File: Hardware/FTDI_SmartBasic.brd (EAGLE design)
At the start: 35.6 x 20.3 mm, 29 parts, among them U1 FT232RLSSOP, U2 MIC5219 3.3V, U3 TS3USB221A

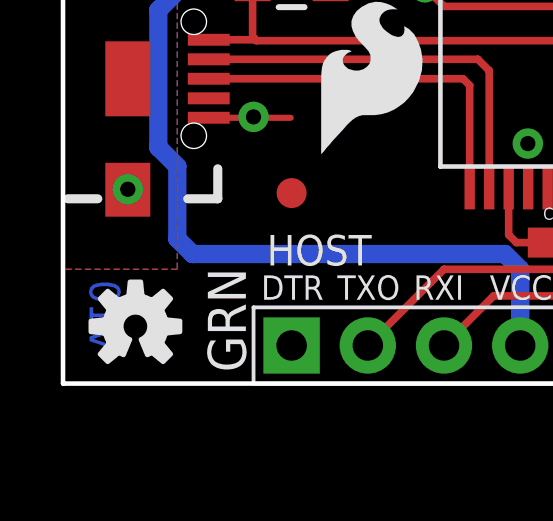
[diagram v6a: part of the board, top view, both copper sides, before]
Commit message: Fixed bottom silk, rev to 11
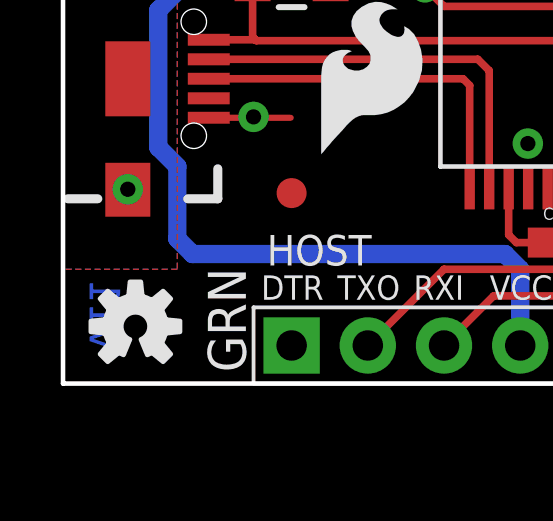
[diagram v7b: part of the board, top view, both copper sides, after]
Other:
- board text added: "v11"
- board text removed: "v10"
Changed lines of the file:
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@@
 <?xml version="1.0" encoding="utf-8"?>
 <!DOCTYPE eagle SYSTEM "eagle.dtd">
-<eagle version="6.6.0">
+<eagle version="6.5.0">
 <drawing>
 <settings>
@@
 <setting verticaltext="up"/>
 </settings>
-<grid distance="0.05" unitdist="inch" unit="inch" style="lines" multiple="1" display="yes" altdistance="0.01" altunitdist="inch" altunit="inch"/>
+<grid distance="0.05" unitdist="inch" unit="inch" style="lines" multiple="1" display="yes" altdistance="0.005" altunitdist="inch" altunit="inch"/>
 <layers>
-<layer number="1" name="Top" color="4" fill="1" visible="yes" active="yes"/>
-<layer number="2" name="Route2" color="1" fill="3" visible="yes" active="yes"/>
-<layer number="15" name="Route15" color="4" fill="6" visible="yes" active="yes"/>
+<layer number="1" name="Top" color="4" fill="1" visible="no" active="yes"/>
+<layer number="2" name="Route2" color="1" fill="3" visible="no" active="yes"/>
+<layer number="15" name="Route15" color="4" fill="6" visible="no" active="yes"/>
 <layer number="16" name="Bottom" color="1" fill="1" visible="yes" active="yes"/>
 <layer number="17" name="Pads" color="2" fill="1" visible="yes" active="yes"/>
@@
 <layer number="19" name="Unrouted" color="6" fill="1" visible="yes" active="yes"/>
 <layer number="20" name="Dimension" color="6" fill="1" visible="yes" active="yes"/>
-<layer number="21" name="tPlace" color="6" fill="1" visible="yes" active="yes"/>
-<layer number="22" name="bPlace" color="6" fill="1" visible="yes" active="yes"/>
-<layer number="23" name="tOrigins" color="15" fill="1" visible="yes" active="yes"/>
+<layer number="21" name="tPlace" color="16" fill="1" visible="no" active="yes"/>
+<layer number="22" name="bPlace" color="14" fill="1" visible="yes" active="yes"/>
+<layer number="23" name="tOrigins" color="15" fill="1" visible="no" active="yes"/>
 <layer number="24" name="bOrigins" color="15" fill="1" visible="yes" active="yes"/>
-<layer number="25" name="tNames" color="7" fill="1" visible="yes" active="yes"/>
-<layer number="26" name="bNames" color="7" fill="1" visible="yes" active="yes"/>
-<layer number="27" name="tValues" color="7" fill="1" visible="yes" active="yes"/>
-<layer number="28" name="bValues" color="7" fill="1" visible="yes" active="yes"/>
-<layer number="29" name="tStop" color="7" fill="3" visible="yes" active="yes"/>
-<layer number="30" name="bStop" color="7" fill="6" visible="yes" active="yes"/>
-<layer number="31" name="tCream" color="7" fill="4" visible="yes" active="yes"/>
-<layer number="32" name="bCream" color="7" fill="5" visible="yes" active="yes"/>
-<layer number="39" name="tKeepout" color="4" fill="11" visible="yes" active="yes"/>
-<layer number="40" name="bKeepout" color="1" fill="11" visible="yes" active="yes"/>
-<layer number="41" name="tRestrict" color="4" fill="10" visible="yes" active="yes"/>
-<layer number="42" name="bRestrict" color="1" fill="10" visible="yes" active="yes"/>
-<layer number="43" name="vRestrict" color="2" fill="10" visible="yes" active="yes"/>
-<layer number="44" name="Drills" color="7" fill="1" visible="yes" active="yes"/>
-<layer number="45" name="Holes" color="7" fill="1" visible="yes" active="yes"/>
-<layer number="46" name="Milling" color="3" fill="1" visible="yes" active="yes"/>
-<layer number="51" name="tDocu" color="6" fill="1" visible="yes" active="yes"/>
-<layer number="52" name="bDocu" color="7" fill="1" visible="yes" active="yes"/>
+<layer number="25" name="tNames" color="7" fill="1" visible="no" active="yes"/>
+<layer number="26" name="bNames" color="7" fill="1" visible="no" active="yes"/>
+<layer number="27" name="tValues" color="7" fill="1" visible="no" active="yes"/>
+<layer number="28" name="bValues" color="7" fill="1" visible="no" active="yes"/>
+<layer number="29" name="tStop" color="7" fill="3" visible="no" active="yes"/>
+<layer number="30" name="bStop" color="7" fill="6" visible="no" active="yes"/>
+<layer number="31" name="tCream" color="7" fill="4" visible="no" active="yes"/>
+<layer number="32" name="bCream" color="7" fill="5" visible="no" active="yes"/>
+<layer number="39" name="tKeepout" color="4" fill="11" visible="no" active="yes"/>
+<layer number="40" name="bKeepout" color="1" fill="11" visible="no" active="yes"/>
+<layer number="41" name="tRestrict" color="4" fill="10" visible="no" active="yes"/>
+<layer number="42" name="bRestrict" color="1" fill="10" visible="no" active="yes"/>
+<layer number="43" name="vRestrict" color="2" fill="10" visible="no" active="yes"/>
+<layer number="44" name="Drills" color="7" fill="1" visible="no" active="yes"/>
+<layer number="45" name="Holes" color="7" fill="1" visible="no" active="yes"/>
+<layer number="46" name="Milling" color="3" fill="1" visible="no" active="yes"/>
+<layer number="51" name="tDocu" color="6" fill="1" visible="no" active="yes"/>
+<layer number="52" name="bDocu" color="7" fill="1" visible="no" active="no"/>
 <layer number="3" name="Route3" color="4" fill="3" visible="no" active="no"/>
 <layer number="4" name="Route4" color="1" fill="4" visible="no" active="no"/>
@@
 <text x="9.652" y="18.796" size="0.8128" layer="21" font="vector" ratio="15" rot="R90" align="bottom-center">3.3V</text>
 <text x="9.652" y="16.383" size="0.8128" layer="21" font="vector" ratio="15" rot="R90" align="bottom-center">5V</text>
-<text x="1.905" y="2.286" size="1.016" layer="16" font="vector" ratio="15" rot="MR270" align="bottom-center">v10</text>
+<text x="1.905" y="2.286" size="1.016" layer="16" font="vector" ratio="15" rot="MR270" align="bottom-center">v11</text>
 <text x="7.62" y="2.54" size="0.8128" layer="22" font="vector" ratio="15" rot="MR0" align="bottom-center">DTR</text>
 <text x="10.16" y="2.54" size="0.8128" layer="22" font="vector" ratio="15" rot="MR0" align="bottom-center">TXO</text>
@@
 <text x="27.94" y="3.048" size="0.8636" layer="22" font="vector" ratio="15" rot="MR0" align="bottom-center">SEL</text>
 <text x="30.48" y="3.048" size="0.8636" layer="22" font="vector" ratio="15" rot="MR0" align="bottom-center">!OE</text>
-<text x="33.02" y="3.81" size="0.8636" layer="22" font="vector" ratio="15" rot="SMR270" align="bottom-center">DTR</text>
-<text x="33.02" y="6.35" size="0.8636" layer="22" font="vector" ratio="15" rot="SMR270" align="bottom-center">RXI</text>
-<text x="33.02" y="8.89" size="0.8636" layer="22" font="vector" ratio="15" rot="SMR270" align="bottom-center">TXO</text>
-<text x="33.02" y="11.43" size="0.8636" layer="22" font="vector" ratio="15" rot="SMR270" align="bottom-center">VCC</text>
-<text x="33.02" y="13.97" size="0.8636" layer="22" font="vector" ratio="15" rot="SMR270" align="bottom-center">CTS</text>
-<text x="33.02" y="16.51" size="0.8636" layer="22" font="vector" ratio="15" rot="SMR270" align="bottom-center">GND</text>
+<text x="33.02" y="16.51" size="0.8636" layer="22" font="vector" ratio="15" rot="SMR270" align="bottom-center">DTR</text>
+<text x="33.02" y="13.97" size="0.8636" layer="22" font="vector" ratio="15" rot="SMR270" align="bottom-center">RXI</text>
+<text x="33.02" y="11.43" size="0.8636" layer="22" font="vector" ratio="15" rot="SMR270" align="bottom-center">TXO</text>
+<text x="33.02" y="8.89" size="0.8636" layer="22" font="vector" ratio="15" rot="SMR270" align="bottom-center">VCC</text>
+<text x="33.02" y="6.35" size="0.8636" layer="22" font="vector" ratio="15" rot="SMR270" align="bottom-center">CTS</text>
+<text x="33.02" y="3.81" size="0.8636" layer="22" font="vector" ratio="15" rot="SMR270" align="bottom-center">GND</text>
 <text x="8.255" y="9.652" size="0.8636" layer="22" font="vector" ratio="15" rot="MR0" align="bottom-center">BY</text>
 <text x="-46.99" y="12.7" size="1.778" layer="51" ratio="15" align="bottom-center">M. Hord</text>
